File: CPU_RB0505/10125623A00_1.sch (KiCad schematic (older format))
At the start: 65 parts, among them IC3 K6R4016C1D-TI10, IC4 ST10F276, IC40 CD74HCT245M, IC41 74HCT1G04GW, IC42 74HCT1G32GW, IC43 74HCT1G32GW, IC44 NC7SZ66, Q1 8MHz, T6 2N7002

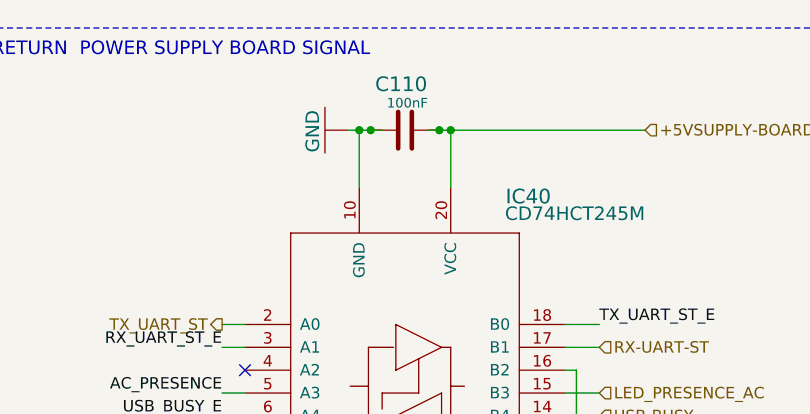
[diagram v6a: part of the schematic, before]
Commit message: Symbols and links update: sch page 4 and global lib
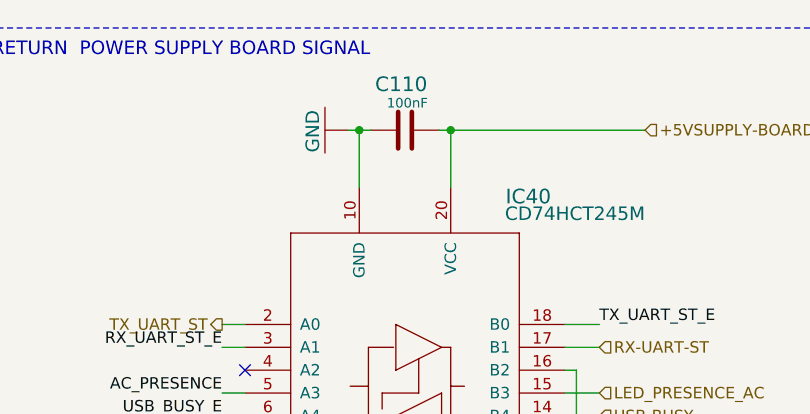
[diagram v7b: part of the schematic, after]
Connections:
- wire segments 592 -> 590
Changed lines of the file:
@@
 $EndComp
 $Comp
-L Capacitor:C0402_100nF_16V_10% C?
-U 1 1 662809D9
-P 11150 1200
-AR Path="/662809D9" Ref="C?"  Part="1"
-AR Path="/5E923584/662809D9" Ref="C110"  Part="1"
-F 0 "C110" V 11388 1069 64  0000 L BNN
-F 1 "100nF" V 11244 1300 42  0000 R TNN
-F 2 "AllModules:C0402_1" H 11150 1200 50  0001 C CNN
-F 3 "" H 11150 1200 50  0001 C CNN
-	1    11150 1200
-	0    1    -1   0
-$EndComp
-$Comp
 L cpu-board:GND #U$?
 U 1 1 5DD0B675
@@
 	4400 10550 4400 10950
 Wire Wire Line
-	11050 1200 11000 1200
-Wire Wire Line
 	10950 1450 10950 1200
 Connection ~ 10950 1200
@@
 	10950 1200 10900 1200
 Wire Wire Line
-	11250 1200 11300 1200
-Wire Wire Line
 	11350 1450 11350 1200
 Connection ~ 11350 1200
@@
 Wire Wire Line
 	14850 2150 14800 2150
-Connection ~ 11000 1200
 Wire Wire Line
 	11000 1200 10950 1200
-Connection ~ 11300 1200
 Wire Wire Line
 	11300 1200 11350 1200
@@
 Wire Wire Line
 	8450 1450 8450 1500
+$Comp
+L Capacitor:C0402_100nF_16V_10% C?
+U 1 1 662809D9
+P 11150 1200
+AR Path="/662809D9" Ref="C?"  Part="1"
+AR Path="/5E923584/662809D9" Ref="C110"  Part="1"
+F 0 "C110" V 11388 1069 64  0000 L BNN
+F 1 "100nF" V 11244 1300 42  0000 R TNN
+F 2 "AllModules:C0402_1" H 11150 1200 50  0001 C CNN
+F 3 "" H 11150 1200 50  0001 C CNN
+	1    11150 1200
+	0    1    -1   0
+$EndComp
 Wire Bus Line
 	15950 2650 15950 4250

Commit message: Symbols and links update: sch page 1 and global lib
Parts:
- C10: Manufacturer4 MURATA MANUFACTURING CO., LTD. -> (none); Manufacturer_Desc4 MONOLITHIC CERAMIC CAPACITOR -> (none); Manufacturer_No4 GRM155R71C104KA88D -> (none)
- C14: symbol Capacitor:RES_4CB -> Capacitor:C0612_47pF_50V_10%
- IC3: symbol cpu-board:K6R4016C1DTCT000(256KX16) -> IC:K6R4016C1DTCT000(256KX16)
- IC4: symbol cpu-board:ST10F269-273-276 -> IC:ST10F269-273-276
- IC40: symbol cpu-board:CD74HCT245M -> IC:CD74HCT245M
- IC41: symbol cpu-board:74HCT1G04GW -> IC:74HCT1G04GW
- IC42, IC43: symbol cpu-board:74HCT1G32GW -> IC:74HCT1G32GW
- IC44: symbol cpu-board:NC7SZ66 -> IC:NC7SZ66
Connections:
- wire segments 590 -> 555
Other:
- moved on the sheet: C1, C3
